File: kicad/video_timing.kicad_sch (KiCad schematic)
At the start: 12 parts, among them U13 ATF22V10C-7PX, U14 ATF22V10C-7PX, U15 ATF22V10C-7PX, U29 SN74F541N, U35 ATF22V10C-7PX

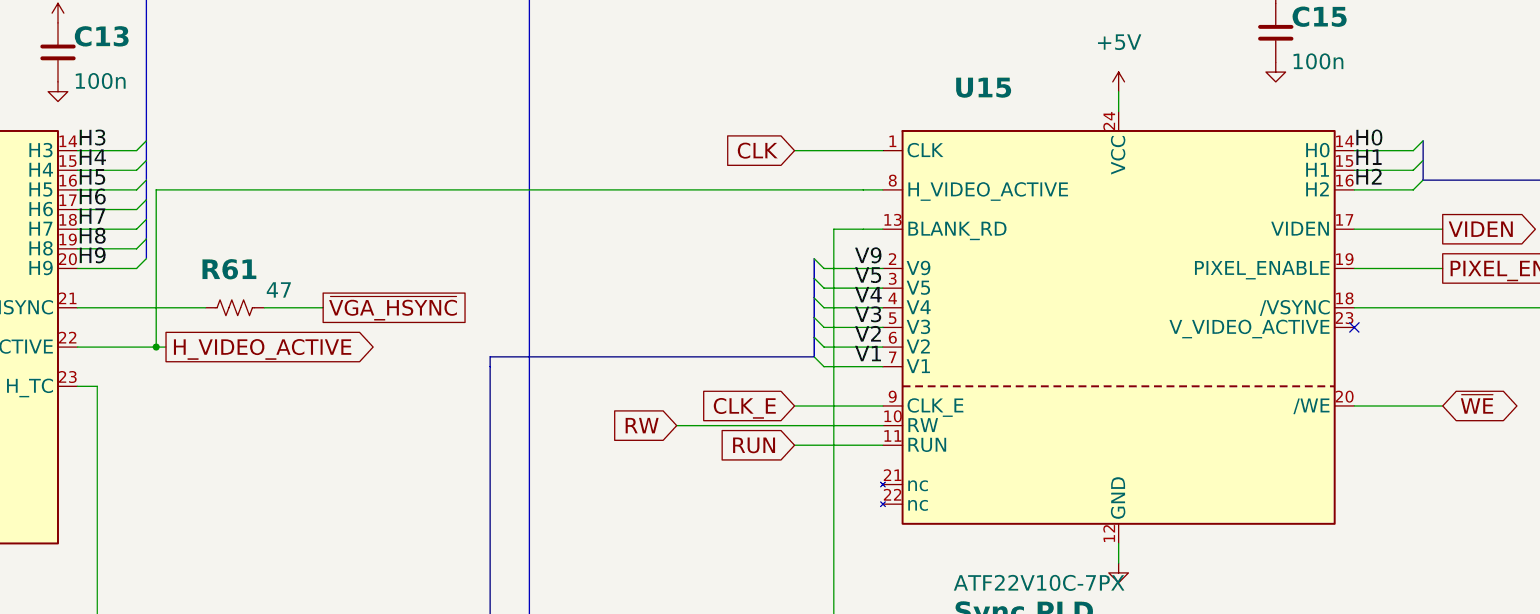
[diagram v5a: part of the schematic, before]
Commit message: Expansion slots use the cartridge's Molex 87715-9106
Justin, 2026-10-30: instead of the 2 x 25 EBC25DRXH (which would have moved
J9-J12 and U38/U42), the four expansion slots take the cartridge's 64-contact
connector.  Every slot has A15:A0, D7:D0, PIXEL_ENABLE, /HSYNC and /VSYNC.
The contacts a cartridge drives are left open, and every expansion output is
on a cartridge-slot spare, so neither does harm in the other's slot.
Footprint Molex_87715-9106_Expansion_Slot keeps the 72 mm card and its keepout
where the 2 x 20 slot had them (connector offset 7.63 mm), so nothing on the
board moves.  Schematic (netlist check 0 problems), symbol, 3D model,
EXPANSION.md pinout, CASE.md, BRINGUP.md, BOM ($199.47), keepout drawing.

Co-Authored-By: Claude Opus 5.5 <noreply@anthropic.com>
Claude-Session: https://claude.ai/code/session_01DnW5SUDtmC2C2nXUS4xVk2
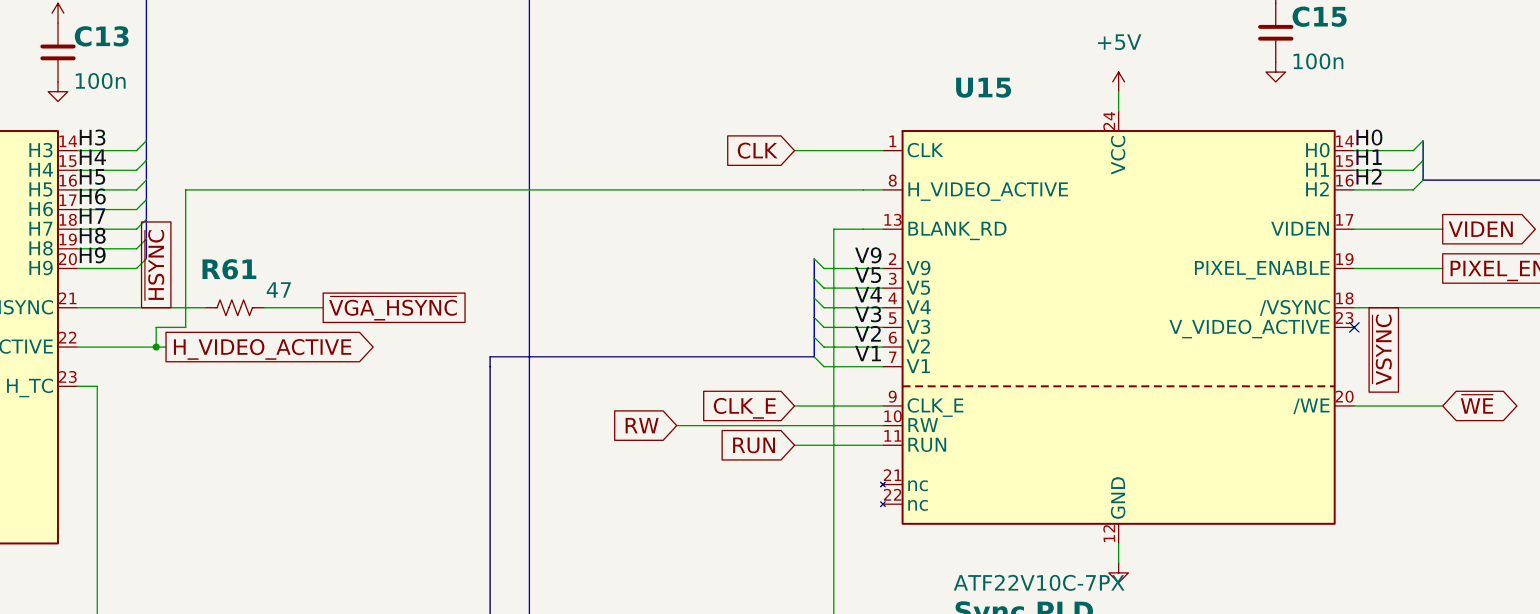
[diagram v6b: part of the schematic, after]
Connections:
- net ~{VSYNC}: now reaches R62.1, U15.18 (/VSYNC)
- net ~{HSYNC}: now reaches R61.1, U13.21 (/HSYNC)
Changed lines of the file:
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@@
   (bus (pts (xy 378.46 153.67) (xy 378.46 156.21)) (stroke (width 0) (type default)))
   (bus (pts (xy 378.46 156.21) (xy 378.46 158.75)) (stroke (width 0) (type default)))
+  (global_label "~{HSYNC}" (shape passive) (at 109.22 96.52 90) (fields_autoplaced) (effects (font (size 2 2)) (justify left)) (property "Intersheetrefs" "${INTERSHEET_REFS}" (at 109.22 96.52 0) (effects (font (size 2 2)) (justify left) hide)))
   (global_label "~{VGA_HSYNC}" (shape passive) (at 130.81 96.52 0) (fields_autoplaced) (effects (font (size 2 2)) (justify left)) (property "Intersheetrefs" "${INTERSHEET_REFS}" (at 130.81 96.52 0) (effects (font (size 2 2)) (justify left) hide)))
+  (global_label "~{VSYNC}" (shape passive) (at 267.97 96.52 270) (fields_autoplaced) (effects (font (size 2 2)) (justify right)) (property "Intersheetrefs" "${INTERSHEET_REFS}" (at 267.97 96.52 0) (effects (font (size 2 2)) (justify left) hide)))
   (global_label "~{VGA_VSYNC}" (shape passive) (at 323.85 96.52 0) (fields_autoplaced) (effects (font (size 2 2)) (justify left)) (property "Intersheetrefs" "${INTERSHEET_REFS}" (at 323.85 96.52 0) (effects (font (size 2 2)) (justify left) hide)))
   (bus (pts (xy 44.45 74.93) (xy 44.45 67.31)) (stroke (width 0) (type default)))
@@
   (bus (pts (xy 378.46 140.97) (xy 378.46 138.43)) (stroke (width 0) (type default)))
   (global_label "DATABUS[0..7]" (shape bidirectional) (at 378.46 138.43 90) (fields_autoplaced) (effects (font (size 2 2)) (justify left)) (property "Intersheetrefs" "${INTERSHEET_REFS}" (at 378.46 138.43 0) (effects (font (size 2 2)) (justify left) hide)))
-  (wire (pts (xy 200.66 81.28) (xy 109.22 81.28)) (stroke (width 0) (type default)))
-  (wire (pts (xy 109.22 81.28) (xy 109.22 101.6)) (stroke (width 0) (type default)))
+  (wire (pts (xy 200.66 81.28) (xy 113.03 81.28)) (stroke (width 0) (type default)))
+  (wire (pts (xy 113.03 81.28) (xy 113.03 99.06)) (stroke (width 0) (type default)))
+  (wire (pts (xy 113.03 99.06) (xy 109.22 99.06)) (stroke (width 0) (type default)))
+  (wire (pts (xy 109.22 99.06) (xy 109.22 101.6)) (stroke (width 0) (type default)))
   (wire (pts (xy 254 200.66) (xy 283.21 200.66)) (stroke (width 0) (type default)))
   (wire (pts (xy 283.21 200.66) (xy 283.21 139.7)) (stroke (width 0) (type default)))

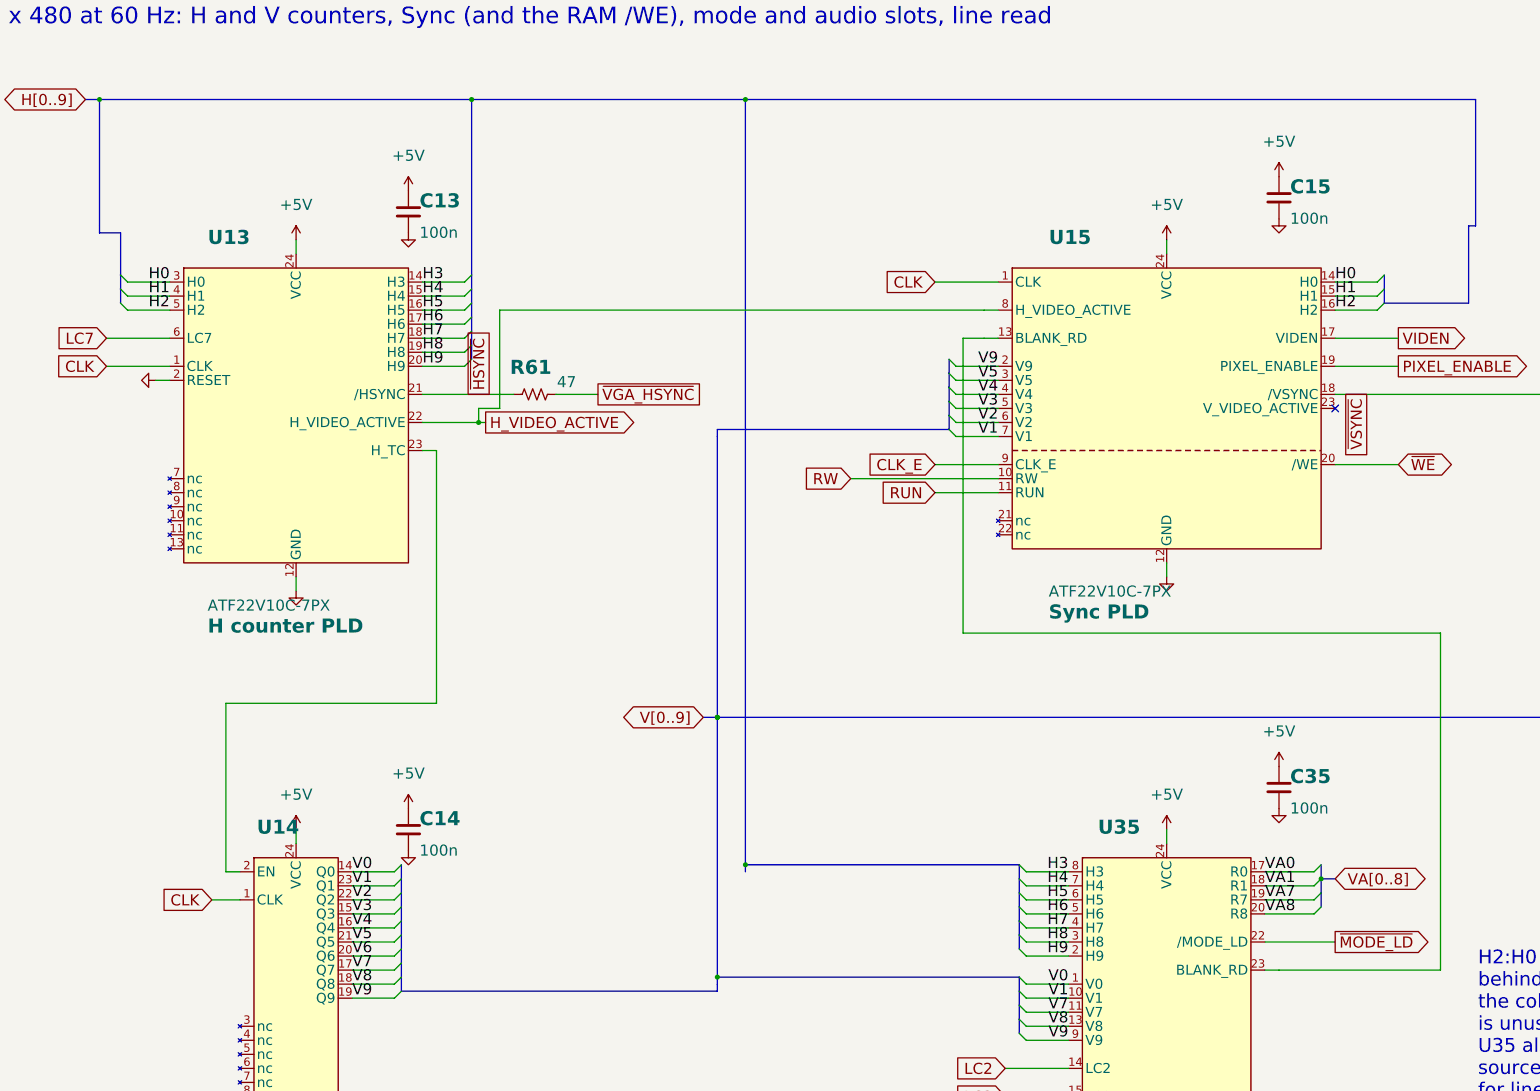
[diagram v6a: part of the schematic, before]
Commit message: Expansion slots: grounds on the inner rows, signals outer; take in Justin's KiCad edits
Reassign the expansion slot contacts so the extra grounds sit on the
inner (even) rows and the signals on the outer (odd) rows wherever the
cartridge pinout allows: 19 of 38 signals outer.  The cartridge's power
and ground contacts, the shared signals and the wrong-slot rules are
kept (every expansion output and extra ground on a J8 spare, every
cartridge output open on the expansion slot).  BT4 and BT6-BT8 dropped.

Justin's local KiCad edits (all main-board sheets, the board and the
project; K1 coil pins swapped) are committed as he saved them; only the
expansion sheet comes from the generator.  Netlist differs from his
only on J9-J12; ERC unchanged.

Co-Authored-By: Claude Opus 5.5 <noreply@anthropic.com>
Claude-Session: https://claude.ai/code/session_01DnW5SUDtmC2C2nXUS4xVk2
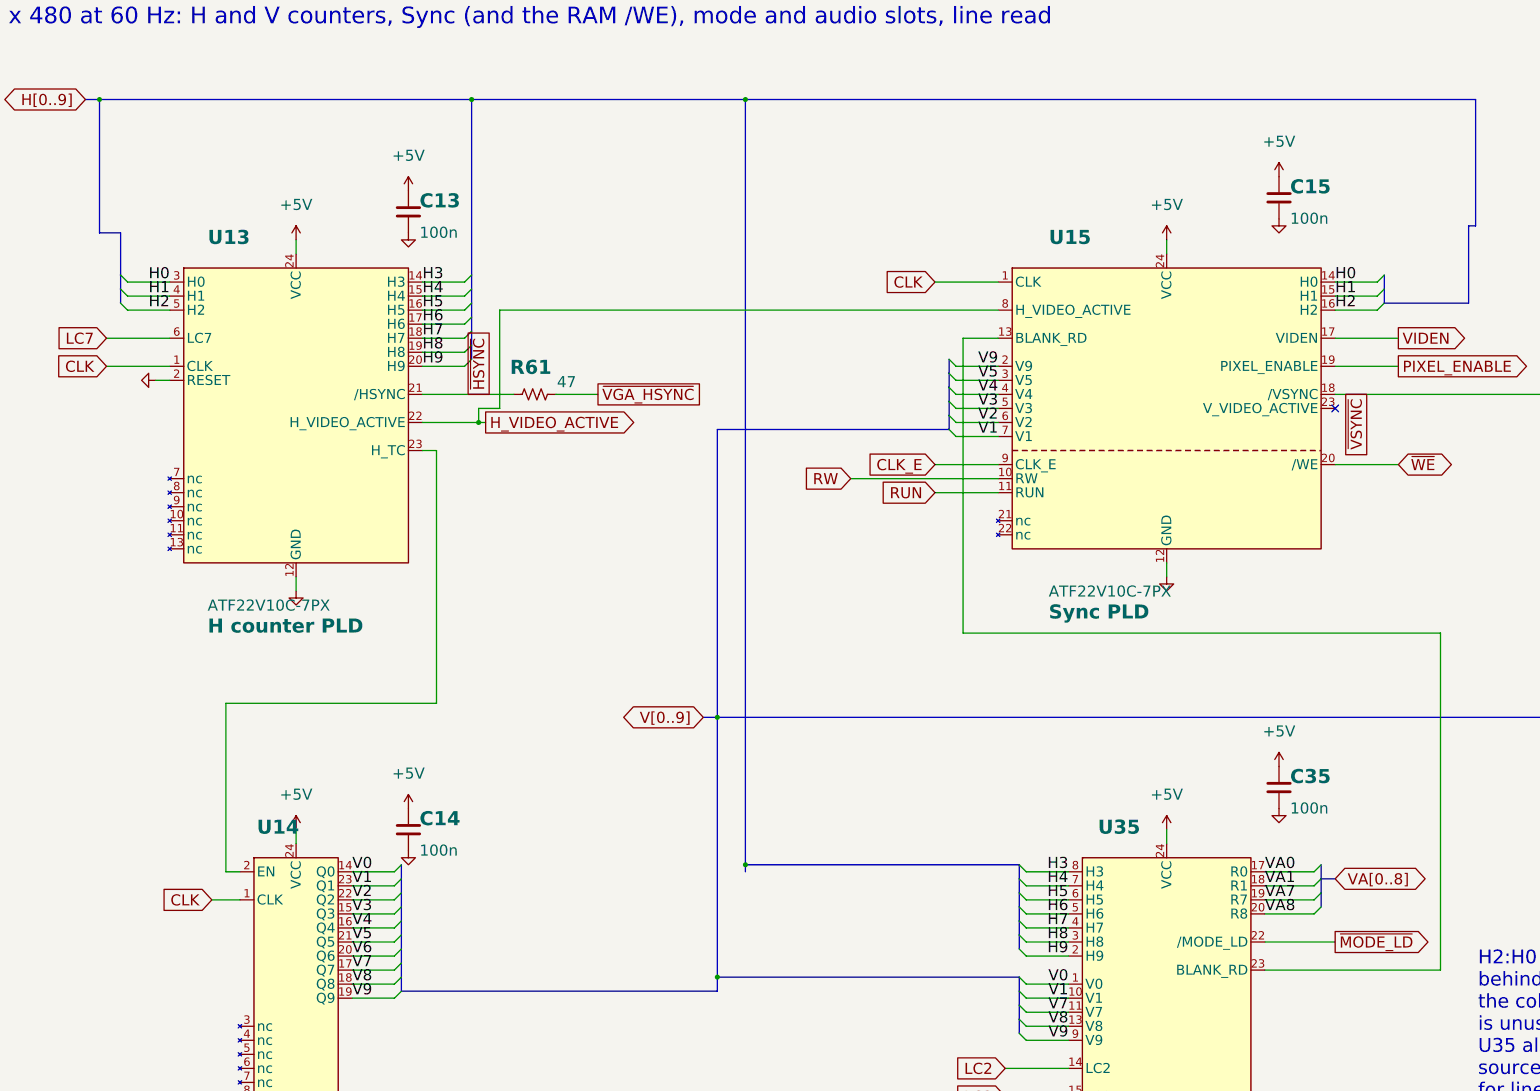
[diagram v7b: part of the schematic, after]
